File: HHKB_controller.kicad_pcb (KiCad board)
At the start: 2 copper layers, 141.5 x 36 mm, 96 parts, among them CN1 CONN_15, CN2 CONN_13, J1 USB_mini_micro_B, P1 GND, P10 CONN_1, P100 CONN_2, P11 CONN_1, P110 CONN_1, P111 CONN_1, P112 CONN_1, P113 CONN_1, P114 CONN_1, P115 CONN_1, P12 CONN_1, P130 CONN_1, P131 CONN_1, P2 D+, P3 D-, P4 VUSB, P5 PD1, P6 PD0, P7 GND, P8 CONN_3X2, P9 CONN_1, Q1 N, Q2 N, Q3 N, Q5 P, SW1 SW_PUSH, SW2 SW_DPDT, U1 ATMEGA32U4, U2 TAR5SB33, U3 NCP1402, U4 MCP73831, U5 RN42, X1 16MHz

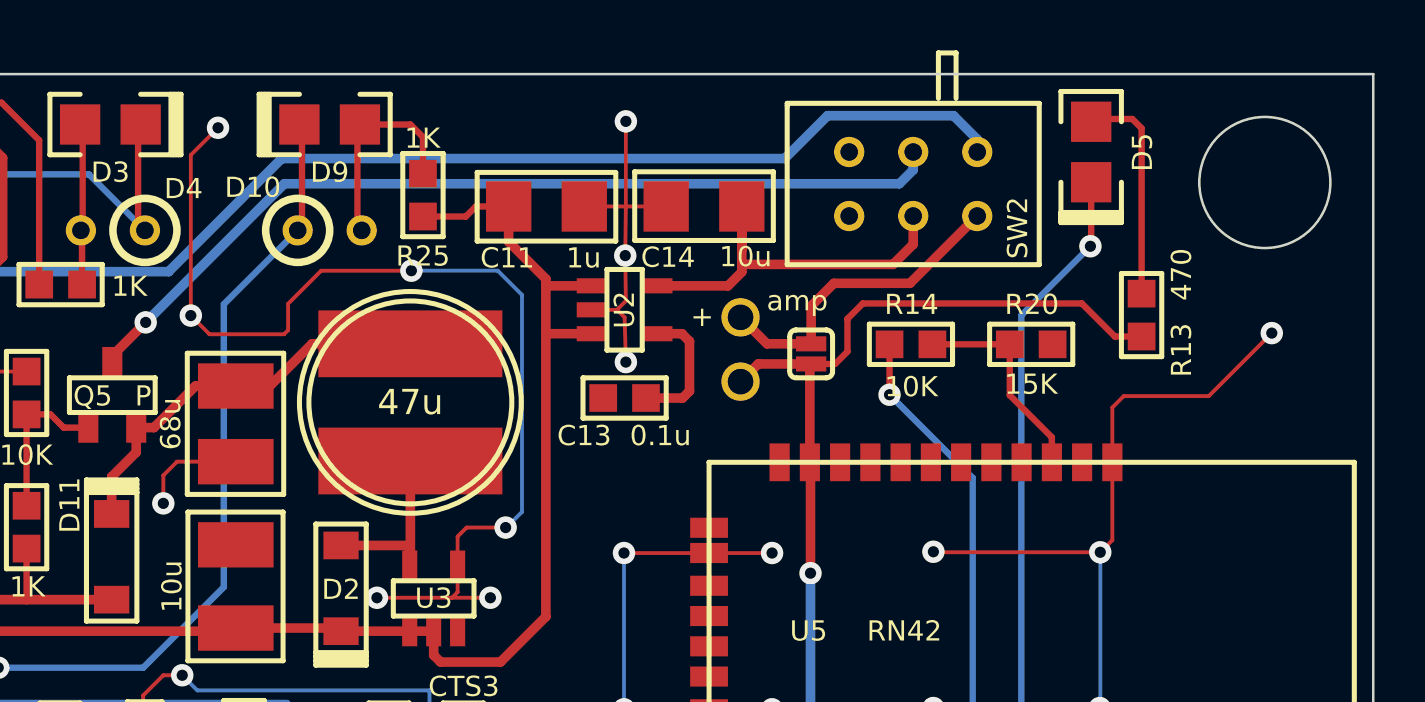
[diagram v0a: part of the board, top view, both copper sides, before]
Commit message: Fix position of right top hole 0.2mm to the right
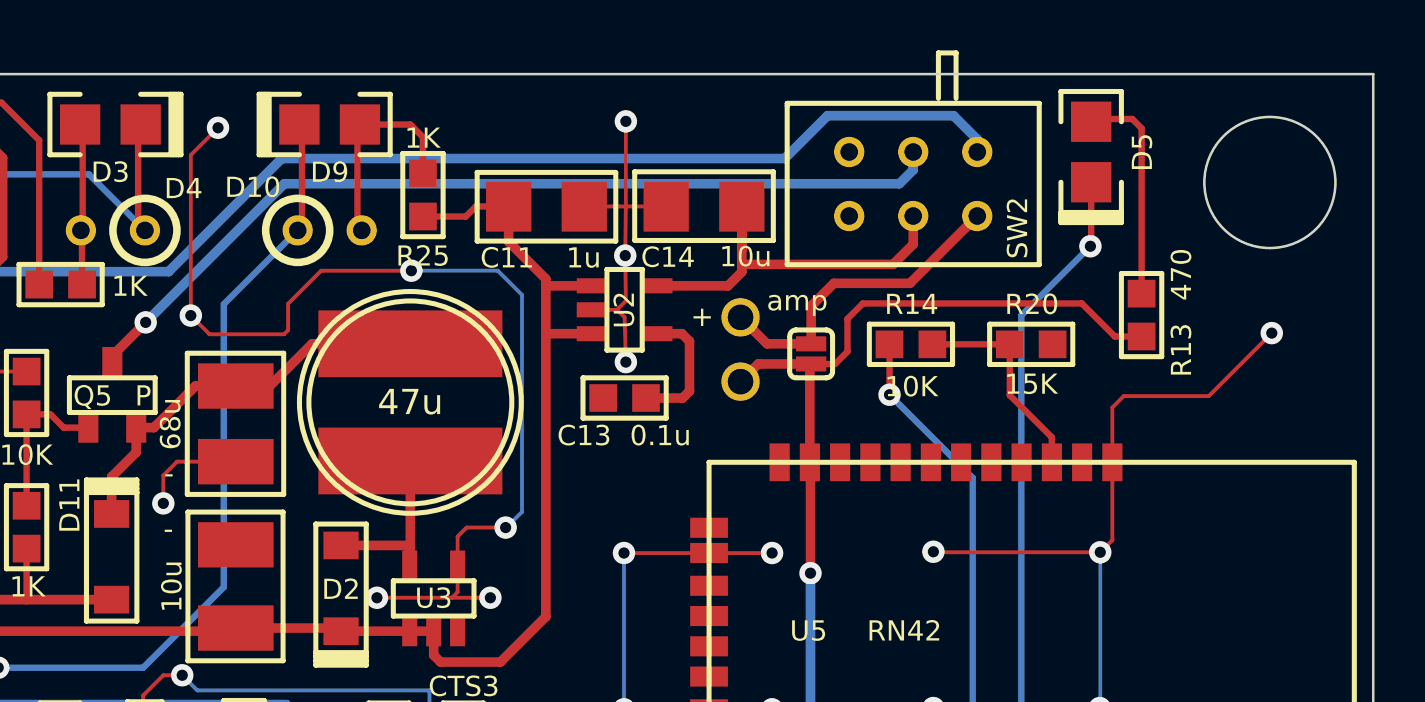
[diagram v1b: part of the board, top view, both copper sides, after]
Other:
- outline, holes or cut-outs redrawn
- board text added: "-"
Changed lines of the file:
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@@
     (area 64.039285 57.7 239.6 122.650001)
     (thickness 1.6)
-    (drawings 94)
+    (drawings 95)
     (tracks 990)
     (zones 0)
@@
     (22 B.Mask user hide)
     (23 F.Mask user hide)
-    (24 Dwgs.User user hide)
-    (25 Cmts.User user hide)
+    (24 Dwgs.User user)
+    (25 Cmts.User user)
     (28 Edge.Cuts user)
   )
@@
     )
   )
+  (dimension 5.2 (width 0.15) (layer Dwgs.User)
+    (gr_text "5.200 mm" (at 220.91 85.1 270) (layer Dwgs.User)
+      (effects (font (size 0.8 0.8) (thickness 0.15)))
+    )
+    (feature1 (pts (xy 214.3 87.7) (xy 221.61 87.7)))
+    (feature2 (pts (xy 214.3 82.5) (xy 221.61 82.5)))
+    (crossbar (pts (xy 220.21 82.5) (xy 220.21 87.7)))
+    (arrow1a (pts (xy 220.21 87.7) (xy 219.623579 86.573496)))
+    (arrow1b (pts (xy 220.21 87.7) (xy 220.796421 86.573496)))
+    (arrow2a (pts (xy 220.21 82.5) (xy 219.623579 83.626504)))
+    (arrow2b (pts (xy 220.21 82.5) (xy 220.796421 83.626504)))
+  )
+  (dimension 4.3 (width 0.15) (layer Dwgs.User)
+    (gr_text "4.300 mm" (at 223.13 82.95 90) (layer Dwgs.User)
+      (effects (font (size 0.8 0.8) (thickness 0.15)))
+    )
+    (feature1 (pts (xy 214.3 80.8) (xy 223.83 80.8)))
+    (feature2 (pts (xy 214.3 85.1) (xy 223.83 85.1)))
+    (crossbar (pts (xy 222.43 85.1) (xy 222.43 80.8)))
+    (arrow1a (pts (xy 222.43 80.8) (xy 223.016421 81.926504)))
+    (arrow1b (pts (xy 222.43 80.8) (xy 221.843579 81.926504)))
+    (arrow2a (pts (xy 222.43 85.1) (xy 223.016421 83.973496)))
+    (arrow2b (pts (xy 222.43 85.1) (xy 221.843579 83.973496)))
+  )
+  (dimension 4.1 (width 0.15) (layer Dwgs.User)
+    (gr_text "4.100 mm" (at 216.35 76.99) (layer Dwgs.User)
+      (effects (font (size 0.8 0.8) (thickness 0.15)))
+    )
+    (feature1 (pts (xy 218.4 85.1) (xy 218.4 76.29)))
+    (feature2 (pts (xy 214.3 85.1) (xy 214.3 76.29)))
+    (crossbar (pts (xy 214.3 77.69) (xy 218.4 77.69)))
+    (arrow1a (pts (xy 218.4 77.69) (xy 217.273496 78.276421)))
+    (arrow1b (pts (xy 218.4 77.69) (xy 217.273496 77.103579)))
+    (arrow2a (pts (xy 214.3 77.69) (xy 215.426504 78.276421)))
+    (arrow2b (pts (xy 214.3 77.69) (xy 215.426504 77.103579)))
+  )
+  (gr_text - (at 170.625 96.65) (layer F.SilkS)
+    (effects (font (size 0.8 0.8) (thickness 0.15)))
+  )
+  (gr_text - (at 170.6 98.85) (layer F.SilkS)
+    (effects (font (size 0.8 0.8) (thickness 0.15)) (justify mirror))
+  )
   (gr_text RX3 (at 182.325 110.425) (layer F.SilkS)
     (effects (font (size 0.8 0.8) (thickness 0.15)))
@@
     (arrow2b (pts (xy 231.4 116.8) (xy 230.813579 115.673496)))
   )
-  (dimension 6.4 (width 0.3) (layer Dwgs.User)
-    (gr_text "6.400 mm" (at 222.45 81.9 90) (layer Dwgs.User)
-      (effects (font (size 1.5 1.5) (thickness 0.3)))
-    )
-    (feature1 (pts (xy 214.1 81.9) (xy 221.75 81.9)))
-    (feature2 (pts (xy 214.1 88.3) (xy 221.75 88.3)))
-    (crossbar (pts (xy 220.35 88.3) (xy 220.35 81.9)))
-    (arrow1a (pts (xy 220.35 81.9) (xy 220.936421 83.026504)))
-    (arrow1b (pts (xy 220.35 81.9) (xy 219.763579 83.026504)))
-    (arrow2a (pts (xy 220.35 88.3) (xy 220.936421 87.173496)))
-    (arrow2b (pts (xy 220.35 88.3) (xy 219.763579 87.173496)))
-  )
-  (gr_circle (center 214.1 85.1) (end 214.15 81.9) (layer Dwgs.User) (width 0.2))
+  (gr_circle (center 214.3 85.1) (end 217.5 85.1) (layer Dwgs.User) (width 0.2))
   (gr_text "No BT" (at 149.575 100.2) (layer F.SilkS)
     (effects (font (size 0.8 0.8) (thickness 0.15)))
@@
   (gr_arc (start 80.1 84.4) (end 80.1 85.9) (angle 90) (layer Edge.Cuts) (width 0.1))
   (gr_arc (start 80.1 84.4) (end 78.6 84.4) (angle 90) (layer Edge.Cuts) (width 0.1))
-  (gr_circle (center 214.1 85.1) (end 216.7 85.1) (layer Edge.Cuts) (width 0.1))
+  (gr_circle (center 214.3 85.1) (end 216.9 85.1) (layer Edge.Cuts) (width 0.1))
   (gr_line (start 151.9 114.3) (end 151.9 116.8) (angle 90) (layer Dwgs.User) (width 0.2))
   (gr_line (start 141.9 114.3) (end 151.9 114.3) (angle 90) (layer Dwgs.User) (width 0.2))
@@
     (arrow2b (pts (xy 92.1 74.200001) (xy 93.226503 73.613581)))
   )
-  (dimension 5.2 (width 0.3) (layer Dwgs.User)
-    (gr_text "5.200 mm" (at 217.5 93.7) (layer Dwgs.User)
-      (effects (font (size 1.5 1.5) (thickness 0.3)))
-    )
-    (feature1 (pts (xy 216.7 85.1) (xy 216.7 94.549999)))
-    (feature2 (pts (xy 211.5 85.1) (xy 211.5 94.549999)))
-    (crossbar (pts (xy 211.5 91.849999) (xy 216.7 91.849999)))
-    (arrow1a (pts (xy 216.7 91.849999) (xy 215.573497 92.436419)))
-    (arrow1b (pts (xy 216.7 91.849999) (xy 215.573497 91.263579)))
-    (arrow2a (pts (xy 211.5 91.849999) (xy 212.626503 92.436419)))
-    (arrow2b (pts (xy 211.5 91.849999) (xy 212.626503 91.263579)))
-  )
-  (dimension 4.3 (width 0.3) (layer Dwgs.User)
-    (gr_text "4.300 mm" (at 228.05 79 90) (layer Dwgs.User)
-      (effects (font (size 1.5 1.5) (thickness 0.3)))
-    )
-    (feature1 (pts (xy 214.1 80.8) (xy 227.8 80.8)))
-    (feature2 (pts (xy 214.1 85.1) (xy 227.8 85.1)))
-    (crossbar (pts (xy 225.1 85.1) (xy 225.1 80.8)))
-    (arrow1a (pts (xy 225.1 80.8) (xy 225.68642 81.926503)))
-    (arrow1b (pts (xy 225.1 80.8) (xy 224.51358 81.926503)))
-    (arrow2a (pts (xy 225.1 85.1) (xy 225.68642 83.973497)))
-    (arrow2b (pts (xy 225.1 85.1) (xy 224.51358 83.973497)))
-  )
-  (dimension 4.3 (width 0.3) (layer Dwgs.User)
-    (gr_text "4.300 mm" (at 216.25 75.450001) (layer Dwgs.User)
-      (effects (font (size 1.5 1.5) (thickness 0.3)))
-    )
-    (feature1 (pts (xy 218.4 85.1) (xy 218.4 74.100001)))
-    (feature2 (pts (xy 214.1 85.1) (xy 214.1 74.100001)))
-    (crossbar (pts (xy 214.1 76.800001) (xy 218.4 76.800001)))
-    (arrow1a (pts (xy 218.4 76.800001) (xy 217.273497 77.386421)))
-    (arrow1b (pts (xy 218.4 76.800001) (xy 217.273497 76.213581)))
-    (arrow2a (pts (xy 214.1 76.800001) (xy 215.226503 77.386421)))
-    (arrow2b (pts (xy 214.1 76.800001) (xy 215.226503 76.213581)))
-  )
   (dimension 1 (width 0.15) (layer Dwgs.User)

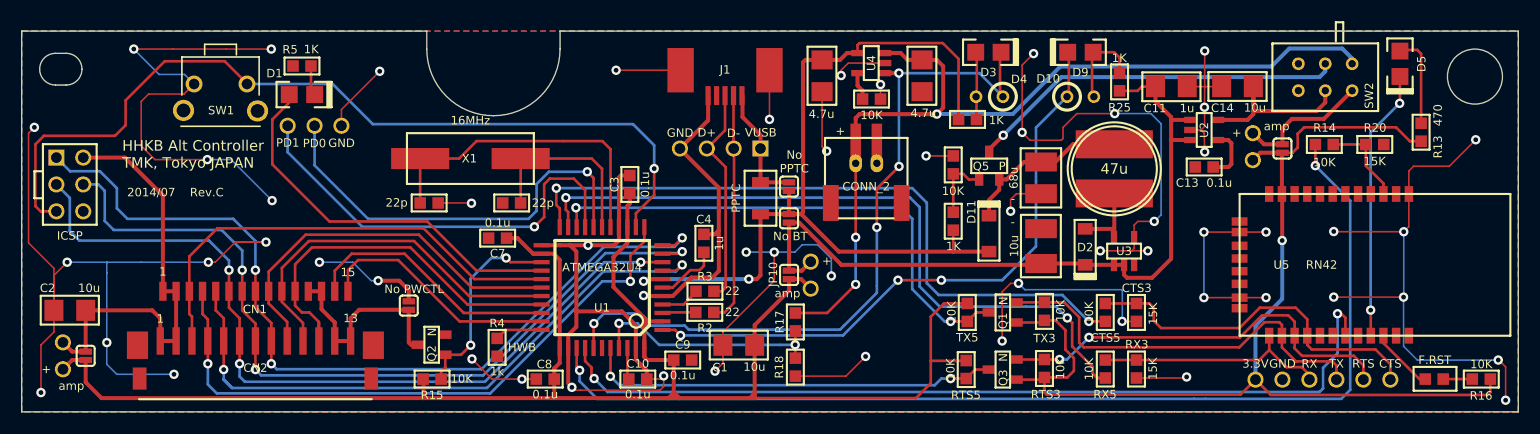
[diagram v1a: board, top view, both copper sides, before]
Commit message: Change drill size for switch and LEDs and minor silk fix
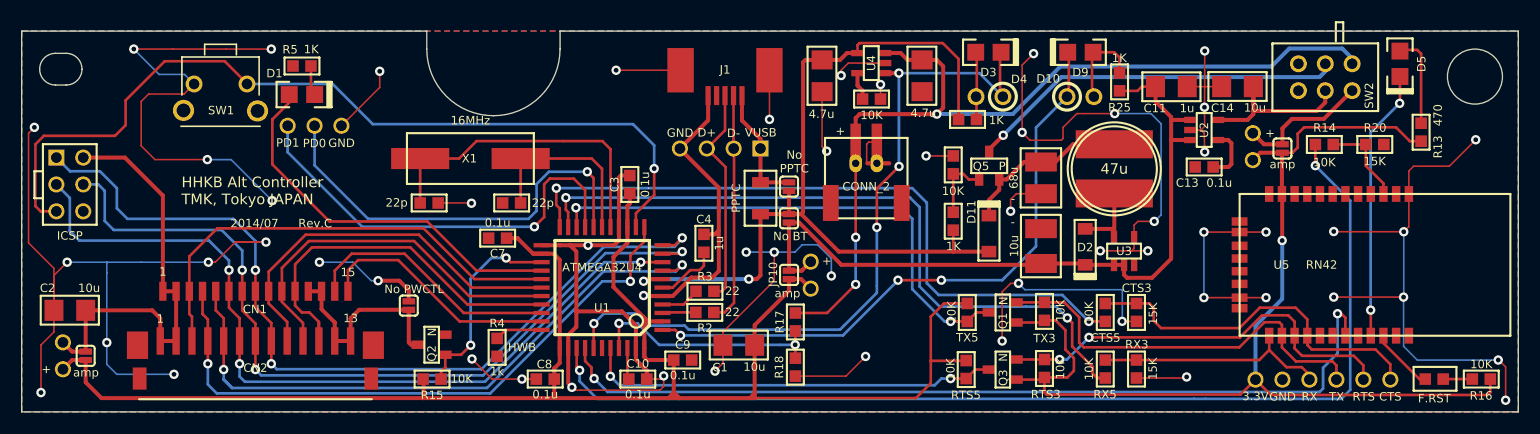
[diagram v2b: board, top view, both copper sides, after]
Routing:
- net GND: track 438.3 -> 440.8 mm
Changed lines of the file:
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@@
     (thickness 1.6)
     (drawings 95)
-    (tracks 990)
+    (tracks 994)
     (zones 0)
     (modules 96)
@@
     (22 B.Mask user hide)
     (23 F.Mask user hide)
-    (24 Dwgs.User user)
-    (25 Cmts.User user)
+    (24 Dwgs.User user hide)
+    (25 Cmts.User user hide)
     (28 Edge.Cuts user)
   )
@@
     (user_trace_width 0.254)
     (user_trace_width 0.381)
+    (user_trace_width 0.4)
     (trace_clearance 0.254)
     (zone_clearance 0.254)
@@
     (mod_text_size 0.8 0.8)
     (mod_text_width 0.15)
-    (pad_size 1.524 1.524)
-    (pad_drill 1.016)
+    (pad_size 1.6 1.6)
+    (pad_drill 1)
     (pad_to_mask_clearance 0)
     (aux_axis_origin 76.9 80.8)
@@
       (drillshape 0)
       (scaleselection 1)
-      (outputdirectory plot/))
+      (outputdirectory plot/C0))
   )
   (net 0 "")
@@
     )
     (fp_circle (center 1.27 0) (end 1.27 -1.27) (layer F.SilkS) (width 0.3))
-    (pad 1 thru_hole circle (at -1.27 0) (size 1.2 1.2) (drill 0.7) (layers *.Cu *.Mask F.SilkS)
+    (pad 1 thru_hole circle (at -1.27 0) (size 1.6 1.6) (drill 1) (layers *.Cu *.Mask F.SilkS)
       (net 48 "Net-(D3-Pad1)"))
-    (pad 2 thru_hole circle (at 1.27 0) (size 1.2 1.2) (drill 0.7) (layers *.Cu *.Mask F.SilkS)
+    (pad 2 thru_hole circle (at 1.27 0) (size 1.6 1.6) (drill 1) (layers *.Cu *.Mask F.SilkS)
       (net 58 ~CHRG))
     (model discret/leds/led3_vertical_verde.wrl
@@
     )
     (fp_circle (center 1.27 0) (end 1.27 -1.27) (layer F.SilkS) (width 0.3))
-    (pad 1 thru_hole circle (at -1.27 0 180) (size 1.2 1.2) (drill 0.7) (layers *.Cu *.Mask F.SilkS)
+    (pad 1 thru_hole circle (at -1.27 0 180) (size 1.6 1.6) (drill 1) (layers *.Cu *.Mask F.SilkS)
       (net 50 "Net-(D10-Pad1)"))
-    (pad 2 thru_hole circle (at 1.27 0 180) (size 1.2 1.2) (drill 0.7) (layers *.Cu *.Mask F.SilkS)
+    (pad 2 thru_hole circle (at 1.27 0 180) (size 1.6 1.6) (drill 1) (layers *.Cu *.Mask F.SilkS)
       (net 35 BT_INDICATOR))
     (model discret/leds/led3_vertical_verde.wrl
@@
     (fp_line (start 5 3.2) (end -5 3.2) (layer F.SilkS) (width 0.2))
     (fp_line (start -5 3.2) (end -5 -3.1) (layer F.SilkS) (width 0.2))
-    (pad 3 thru_hole circle (at -2.54 -1.27) (size 1.2 1.2) (drill 0.7) (layers *.Cu *.Mask F.SilkS))
-    (pad 2 thru_hole circle (at 2.54 -1.27) (size 1.2 1.2) (drill 0.7) (layers *.Cu *.Mask F.SilkS)
+    (pad 3 thru_hole circle (at -2.54 -1.27) (size 1.6 1.6) (drill 1) (layers *.Cu *.Mask F.SilkS))
+    (pad 2 thru_hole circle (at 2.54 -1.27) (size 1.6 1.6) (drill 1) (layers *.Cu *.Mask F.SilkS)
       (net 26 /bluetooth/LIPO_RAW))
-    (pad 1 thru_hole circle (at 0 -1.27) (size 1.2 1.2) (drill 0.7) (layers *.Cu *.Mask F.SilkS)
+    (pad 1 thru_hole circle (at 0 -1.27) (size 1.6 1.6) (drill 1) (layers *.Cu *.Mask F.SilkS)
       (net 27 /bluetooth/LIPO_SW))
-    (pad 4 thru_hole circle (at 0 1.27) (size 1.2 1.2) (drill 0.7) (layers *.Cu *.Mask F.SilkS)
+    (pad 4 thru_hole circle (at 0 1.27) (size 1.6 1.6) (drill 1) (layers *.Cu *.Mask F.SilkS)
       (net 22 /bluetooth/3.3V_OUT))
-    (pad 5 thru_hole circle (at 2.54 1.27) (size 1.2 1.2) (drill 0.7) (layers *.Cu *.Mask F.SilkS)
+    (pad 5 thru_hole circle (at 2.54 1.27) (size 1.6 1.6) (drill 1) (layers *.Cu *.Mask F.SilkS)
       (net 1 +3.3V))
-    (pad 6 thru_hole circle (at -2.54 1.27) (size 1.2 1.2) (drill 0.7) (layers *.Cu *.Mask F.SilkS))
+    (pad 6 thru_hole circle (at -2.54 1.27) (size 1.6 1.6) (drill 1) (layers *.Cu *.Mask F.SilkS))
   )
   (module SOLDER_JUMPER_2 (layer F.Cu)
@@
     (effects (font (size 1 1) (thickness 0.25)) (justify left mirror))
   )
-  (gr_text "HHKB Alt Controller\nTMK, Tokyo JAPAN" (at 86.4 92.45) (layer F.SilkS)
+  (gr_text "HHKB Alt Controller\nTMK, Tokyo JAPAN" (at 92.01 95.9) (layer F.SilkS)
     (effects (font (size 1 1) (thickness 0.25)) (justify left))
   )
@@
     (effects (font (size 0.8 0.8) (thickness 0.15)))
   )
-  (gr_text + (at 191.75 90.45 90) (layer F.SilkS)
+  (gr_text + (at 194.9 90.48 90) (layer F.SilkS)
     (effects (font (size 0.8 0.8) (thickness 0.15)))
   )
-  (gr_text amp (at 195.55 89.8) (layer F.SilkS)
+  (gr_text amp (at 196.1 93.4) (layer F.SilkS)
     (effects (font (size 0.8 0.8) (thickness 0.15)))
   )
-  (gr_text amp (at 81.6 114.35) (layer F.SilkS)
+  (gr_text amp (at 82.98 113.09) (layer F.SilkS)
     (effects (font (size 0.8 0.8) (thickness 0.15)))
   )
-  (gr_text F.RST (at 210.5 111.9) (layer F.SilkS)
+  (gr_text F.RST (at 210.46 115.53) (layer F.SilkS)
     (effects (font (size 0.8 0.8) (thickness 0.15)))
   )
-  (gr_text CTS (at 206.3 112.25) (layer F.SilkS)
+  (gr_text CTS (at 206.3 115.36) (layer F.SilkS)
     (effects (font (size 0.8 0.8) (thickness 0.15)))
   )
-  (gr_text RTS (at 203.75 112.25) (layer F.SilkS)
+  (gr_text RTS (at 203.78 115.36) (layer F.SilkS)
     (effects (font (size 0.8 0.8) (thickness 0.15)))
   )
-  (gr_text TX (at 201.2 112.25) (layer F.SilkS)
+  (gr_text TX (at 201.22 115.36) (layer F.SilkS)
     (effects (font (size 0.8 0.8) (thickness 0.15)))
   )
-  (gr_text RX (at 198.65 112.25) (layer F.SilkS)
+  (gr_text RX (at 198.66 115.36) (layer F.SilkS)
     (effects (font (size 0.8 0.8) (thickness 0.15)))
   )
-  (gr_text GND (at 196.1 112.25) (layer F.SilkS)
+  (gr_text GND (at 196.11 115.36) (layer F.SilkS)
     (effects (font (size 0.8 0.8) (thickness 0.15)))
   )
-  (gr_text 3.3V (at 193.55 112.25) (layer F.SilkS)
+  (gr_text 3.3V (at 193.55 115.32) (layer F.SilkS)
     (effects (font (size 0.8 0.8) (thickness 0.2)))
   )
@@
     (arrow2b (pts (xy 207.4 73) (xy 208.526504 72.413579)))
   )
-  (gr_text Rev.C (at 94.4 96.05) (layer F.SilkS)
+  (gr_text Rev.C (at 104.65 98.98) (layer F.SilkS)
     (effects (font (size 0.8 0.8) (thickness 0.15)))
   )
-  (gr_text 2014/07 (at 89.15 96.05) (layer F.SilkS)
+  (gr_text 2014/07 (at 98.91 98.98) (layer F.SilkS)
     (effects (font (size 0.8 0.8) (thickness 0.15)))
   )
@@
   (segment (start 92.75 102.1) (end 92.75 105.4) (width 0.254) (layer F.Cu) (net 20))
   (segment (start 126.055 104.2479) (end 119.6979 104.2479) (width 0.254) (layer F.Cu) (net 20))
-  (segment (start 145.05 88.927) (end 146.756 90.633) (width 0.381) (layer F.Cu) (net 21))
-  (segment (start 146.756 90.633) (end 146.756 91.903) (width 0.381) (layer F.Cu) (net 21))
-  (segment (start 145.05 86.9) (end 145.05 88.927) (width 0.381) (layer F.Cu) (net 21))
   (segment (start 146.75 95.1) (end 146.75 91.9) (width 0.381) (layer F.Cu) (net 21))
   (segment (start 149.45 95.1) (end 146.75 95.1) (width 0.381) (layer F.Cu) (net 21))
+  (segment (start 145 89.24) (end 146.75 90.99) (width 0.381) (layer F.Cu) (net 21))
+  (segment (start 146.75 90.99) (end 146.75 91.9) (width 0.381) (layer F.Cu) (net 21))
+  (segment (start 145 86.9) (end 145 89.24) (width 0.381) (layer F.Cu) (net 21))
   (segment (start 193.35 87.75) (end 193.35 86.05) (width 0.381) (layer F.Cu) (net 22))
   (segment (start 193.35 87.75) (end 193.35 86.05) (width 0.381) (layer F.Cu) (net 22))
@@
   (segment (start 188.675 99.8) (end 188.675 106) (width 0.1524) (layer B.Cu) (net 39))
   (via (at 188.675 99.8) (size 0.889) (layers F.Cu B.Cu) (net 39))
-  (segment (start 107.13 89.75) (end 107.13 88.22) (width 0.1524) (layer F.Cu) (net 39))
-  (via (at 110.75 84.6) (size 0.889) (layers F.Cu B.Cu) (net 39))
-  (segment (start 107.13 88.22) (end 110.75 84.6) (width 0.1524) (layer F.Cu) (net 39))
   (segment (start 94.45 92.95) (end 96.7 92.95) (width 0.1524) (layer B.Cu) (net 39))
   (via (at 94.45 92.95) (size 0.889) (layers F.Cu B.Cu) (net 39))
@@
   (segment (start 79.95 103.225) (end 77.55 100.825) (width 0.1524) (layer F.Cu) (net 39))
   (via (at 100.5 82.5) (size 0.889) (layers F.Cu B.Cu) (net 39))
-  (segment (start 107.13 89.75) (end 107.13 89.345) (width 0.1524) (layer F.Cu) (net 39))
   (segment (start 119.425 97.075) (end 119.4 97.075) (width 0.1524) (layer B.Cu) (net 39))
   (via (at 119.425 97.075) (size 0.889) (layers F.Cu B.Cu) (net 39))
@@
   (segment (start 170.4 104.65) (end 169.6 105.45) (width 0.1524) (layer F.Cu) (net 39))
   (segment (start 171.15 104.65) (end 170.4 104.65) (width 0.1524) (layer F.Cu) (net 39))
-  (segment (start 157.75 93.3) (end 157.75 91.3) (width 0.381) (layer F.Cu) (net 39))
   (segment (start 208.05 99.29) (end 207.57 99.77) (width 0.1524) (layer F.Cu) (net 39))
   (via (at 207.57 99.77) (size 0.889) (layers F.Cu B.Cu) (net 39))
@@
   (segment (start 180.96 108.22) (end 180.96 105.25) (width 0.1524) (layer B.Cu) (net 39))
   (segment (start 182.3 108.25) (end 180.95 108.25) (width 0.1524) (layer F.Cu) (net 39))
+  (segment (start 110.75 86.13) (end 107.13 89.75) (width 0.1524) (layer F.Cu) (net 39))
+  (via (at 110.75 84.6) (size 0.889) (layers F.Cu B.Cu) (net 39))
+  (segment (start 110.75 84.6) (end 110.75 86.13) (width 0.1524) (layer F.Cu) (net 39))
+  (segment (start 157.75 93.3) (end 158.93 93.3) (width 0.4) (layer F.Cu) (net 39))
+  (segment (start 156.85 93.3) (end 157.75 93.3) (width 0.4) (layer F.Cu) (net 39))
+  (segment (start 156.79 93.24) (end 156.85 93.3) (width 0.1524) (layer F.Cu) (net 39))
+  (segment (start 156.79 91.49) (end 156.79 93.24) (width 0.1524) (layer F.Cu) (net 39))
+  (segment (start 156.98 91.3) (end 156.79 91.49) (width 0.1524) (layer F.Cu) (net 39))
+  (segment (start 157.75 91.3) (end 156.98 91.3) (width 0.1524) (layer F.Cu) (net 39))
   (via (at 150.03 110.46) (size 0.889) (layers F.Cu B.Cu) (net 40))
   (segment (start 148.61 110.47) (end 150.02 110.47) (width 0.254) (layer B.Cu) (net 40))
